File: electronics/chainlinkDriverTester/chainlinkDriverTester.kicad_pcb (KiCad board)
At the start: 2 copper layers, 198.1 x 30.5 mm, 69 parts, among them J1 Inputs, J10 Sensor C, J11 Sensor D, J12 Motor E, J13 Motor F, J14 Sensor E, J15 Sensor F, J16 Power, J17 Power, J18 Power, J19 Outputs, J2 Inputs, J20 Outputs, J21 Outputs, J3 Motor A, J4 Inputs, J5 Motor B, J6 Motor C, J7 Motor D, J8 Sensor A, J9 Sensor B, U1 74HC595, U10 TPL7407L, U2 TPL7407L, U3 74HC125, U4 74HC165, U5 74HC595, U6 TPL7407L, U7 74HC595, U8 TPL7407L, U9 74HC595

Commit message: Checkpoint
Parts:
- removed C10, C11, C12, C9: 0.1uF, Capacitor_SMD:C_0603_1608Metric
- removed C8: 10uF, Capacitor_SMD:CP_Elec_4x5.3
- removed D4: LED D, ModifiedSymbols:LED_0603_1608Metric_Silkscreen
- removed D5: LED E, ModifiedSymbols:LED_0603_1608Metric_Silkscreen
- removed D6: LED F, ModifiedSymbols:LED_0603_1608Metric_Silkscreen
- removed J1, J2, J4: Inputs, ScrewTerminals:C8465_WJ500V-5.08-2P
- removed J16, J17, J18: Power, ScrewTerminals:C8465_WJ500V-5.08-2P
- removed J19, J20, J21: Outputs, ScrewTerminals:C8465_WJ500V-5.08-2P
- removed R13: 0R, Resistor_SMD:R_0603_1608Metric
- removed U10, U6, U8: TPL7407L, ModifiedSymbols:SOIC-16_3.9x9.9mm_P1.27mm_silk
- removed U7, U9: 74HC595, ModifiedSymbols:SOIC-16_3.9x9.9mm_P1.27mm_silk
- added F1: 50mA (0ZCM0005FF2G), Fuse:Fuse_0603_1608Metric, F.Cu at (115.6, 105.4)
- added F2: Fuse Holder BK-6013, BK-6013:BK-6013, F.Cu at (120.7, 35.6)
- added H10: MountingHole, MountingHole:MountingHole_3.2mm_M3_ISO7380_Pad, F.Cu at (31.8, 68.6)
- added H11: MountingHole, MountingHole:MountingHole_3.2mm_M3_ISO7380_Pad, F.Cu at (91.4, 68.6)
- added H12: MountingHole, MountingHole:MountingHole_3.2mm_M3_ISO7380_Pad, F.Cu at (124.5, 68.6)
- added H13: MountingHole, MountingHole:MountingHole_3.2mm_M3_ISO7380_Pad, F.Cu at (157.5, 68.6)
- added H14: MountingHole, MountingHole:MountingHole_3.2mm_M3_ISO7380_Pad, F.Cu at (217.2, 68.6)
- added H15: MountingHole, MountingHole:MountingHole_3.2mm_M3_ISO7380_Pad, F.Cu at (124.5, 29.2)
- added H16: MountingHole, MountingHole:MountingHole_3.2mm_M3_ISO7380_Pad, F.Cu at (124.5, 116.8)
- added H8: MountingHole, MountingHole:MountingHole_3.2mm_M3_ISO7380_Pad, F.Cu at (29.2, 116.8)
- added H9: MountingHole, MountingHole:MountingHole_3.2mm_M3_ISO7380_Pad, F.Cu at (219.7, 116.8)
- added J22: Power, ScrewTerminals:C8465_WJ500V-5.08-2P, F.Cu at (108.0, 34.3)
- added J26: exp, Connector_PinHeader_2.54mm:PinHeader_1x04_P2.54mm_Vertical, F.Cu at (134.6, 108.6)
- added J27: exp, Connector_PinHeader_2.54mm:PinHeader_1x04_P2.54mm_Vertical, F.Cu at (134.6, 111.1)
- added J28: exp, Connector_PinHeader_2.54mm:PinHeader_1x04_P2.54mm_Vertical, F.Cu at (134.6, 113.7)
- added J29: exp, Connector_PinHeader_2.54mm:PinHeader_1x04_P2.54mm_Vertical, F.Cu at (147.3, 108.6)
- added J30: exp, Connector_PinHeader_2.54mm:PinHeader_1x04_P2.54mm_Vertical, F.Cu at (147.3, 111.1)
- added J31: exp, Connector_PinHeader_2.54mm:PinHeader_1x04_P2.54mm_Vertical, F.Cu at (147.3, 113.7)
- added J32: Conn_01x06_Female, Connector_PinSocket_2.54mm:PinSocket_1x06_P2.54mm_Vertical, F.Cu at (28.6, 36.8)
- added TP1: TestPoint, pogoPins:pogo1mm, F.Cu at (198.1, 74.9)
- added TP10: TestPoint, pogoPins:pogo1mm, F.Cu at (200.7, 57.1)
- added TP11: TestPoint, pogoPins:pogo1mm, F.Cu at (181.6, 57.1)
- added TP12: TestPoint, pogoPins:pogo1mm, F.Cu at (162.6, 57.1)
- added TP13: TestPoint, pogoPins:pogo1mm, F.Cu at (96.5, 57.1)
- added TP14: TestPoint, pogoPins:pogo1mm, F.Cu at (77.5, 57.1)
- added TP15: TestPoint, pogoPins:pogo1mm, F.Cu at (58.4, 57.1)
- added TP16: TestPoint, pogoPins:pogo1mm, F.Cu at (198.2, 57.1)
- added TP17: TestPoint, pogoPins:pogo1mm, F.Cu at (179.1, 57.1)
- added TP18: TestPoint, pogoPins:pogo1mm, F.Cu at (160.1, 57.1)
- added TP19: TestPoint, pogoPins:pogo1mm, F.Cu at (94.0, 57.1)
- added TP2: TestPoint, pogoPins:pogo1mm, F.Cu at (195.6, 74.9)
- added TP20: TestPoint, pogoPins:pogo1mm, F.Cu at (75.0, 57.1)
- added TP21: TestPoint, pogoPins:pogo1mm, F.Cu at (55.9, 57.1)
- added TP22: TestPoint, pogoPins:pogo1mm, F.Cu at (94.0, 74.9)
- added TP23: TestPoint, pogoPins:pogo1mm, F.Cu at (195.7, 57.1)
- added TP24: TestPoint, pogoPins:pogo1mm, F.Cu at (176.6, 57.1)
- added TP25: TestPoint, pogoPins:pogo1mm, F.Cu at (157.6, 57.1)
- added TP26: TestPoint, pogoPins:pogo1mm, F.Cu at (91.5, 57.1)
- added TP27: TestPoint, pogoPins:pogo1mm, F.Cu at (72.5, 57.1)
- added TP28: TestPoint, pogoPins:pogo1mm, F.Cu at (53.4, 57.1)
- added TP29: TestPoint, pogoPins:pogo1mm, F.Cu at (91.4, 74.9)
- added TP3: TestPoint, pogoPins:pogo1mm, F.Cu at (193.0, 74.9)
- added TP30: TestPoint, pogoPins:pogo1mm, F.Cu at (193.2, 57.1)
- added TP31: TestPoint, pogoPins:pogo1mm, F.Cu at (174.1, 57.1)
- added TP32: TestPoint, pogoPins:pogo1mm, F.Cu at (155.1, 57.1)
- added TP33: TestPoint, pogoPins:pogo1mm, F.Cu at (89.0, 57.1)
- added TP34: TestPoint, pogoPins:pogo1mm, F.Cu at (70.0, 57.1)
- added TP35: TestPoint, pogoPins:pogo1mm, F.Cu at (50.9, 57.1)
- added TP36: TestPoint, pogoPins:pogo1mm, F.Cu at (88.9, 74.9)
- added TP37: TestPoint, pogoPins:pogo1mm, F.Cu at (190.7, 57.1)
- added TP38: TestPoint, pogoPins:pogo1mm, F.Cu at (171.6, 57.1)
- added TP39: TestPoint, pogoPins:pogo1mm, F.Cu at (152.6, 57.1)
- added TP4: TestPoint, pogoPins:pogo1mm, F.Cu at (179.1, 74.9)
- added TP40: TestPoint, pogoPins:pogo1mm, F.Cu at (86.5, 57.1)
- added TP41: TestPoint, pogoPins:pogo1mm, F.Cu at (67.5, 57.1)
- added TP42: TestPoint, pogoPins:pogo1mm, F.Cu at (48.4, 57.1)
- added TP43: TestPoint, pogoPins:pogo1mm, F.Cu at (74.9, 74.9)
- added TP44: TestPoint, pogoPins:pogo1mm, F.Cu at (72.4, 74.9)
- added TP45: TestPoint, pogoPins:pogo1mm, F.Cu at (69.8, 74.9)
- added TP46: TestPoint, pogoPins:pogo1mm, F.Cu at (55.9, 74.9)
- added TP47: TestPoint, pogoPins:pogo1mm, F.Cu at (53.3, 74.9)
- added TP48: TestPoint, pogoPins:pogo1mm, F.Cu at (50.8, 74.9)
- added TP49: TestPoint, pogoPins:pogo2mm, F.Cu at (209.6, 55.9)
- added TP5: TestPoint, pogoPins:pogo1mm, F.Cu at (176.5, 74.9)
- added TP50: TestPoint, pogoPins:pogo2mm, F.Cu at (39.4, 55.9)
- added TP51: TestPoint, pogoPins:pogo2mm, F.Cu at (209.6, 61.0)
- added TP52: TestPoint, pogoPins:pogo2mm, F.Cu at (39.4, 61.0)
- added TP53: TestPoint, pogoPins:pogo2mm, F.Cu at (209.6, 66.0)
- added TP54: TestPoint, pogoPins:pogo2mm, F.Cu at (39.4, 66.0)
- added TP55: TestPoint, pogoPins:pogo2mm, F.Cu at (209.6, 71.1)
- added TP56: TestPoint, pogoPins:pogo2mm, F.Cu at (39.4, 71.1)
- added TP57: TestPoint, pogoPins:pogo2mm, F.Cu at (209.6, 76.2)
- added TP58: TestPoint, pogoPins:pogo2mm, F.Cu at (39.4, 76.2)
- added TP59: TestPoint, pogoPins:pogo2mm, F.Cu at (209.6, 81.3)
- added TP6: TestPoint, pogoPins:pogo1mm, F.Cu at (174.0, 74.9)
- added TP60: TestPoint, pogoPins:pogo2mm, F.Cu at (39.4, 81.3)
- added TP61: TestPoint, TestPoint:TestPoint_THTPad_D2.0mm_Drill1.0mm, F.Cu at (144.8, 92.7)
- added TP62: TestPoint, TestPoint:TestPoint_THTPad_D2.0mm_Drill1.0mm, F.Cu at (142.2, 92.7)
- added TP63: TestPoint, pogoPins:pogo2mm, F.Cu at (111.8, 59.7)
- added TP64: TestPoint, pogoPins:pogo2mm, F.Cu at (116.8, 59.7)
- added TP65: TestPoint, pogoPins:pogo2mm, F.Cu at (121.9, 59.7)
- added TP66: TestPoint, pogoPins:pogo2mm, F.Cu at (127.0, 59.7)
- added TP67: TestPoint, pogoPins:pogo2mm, F.Cu at (132.1, 59.7)
- added TP68: TestPoint, pogoPins:pogo2mm, F.Cu at (137.2, 59.7)
- added TP69: TestPoint, TestPoint:TestPoint_THTPad_D2.0mm_Drill1.0mm, F.Cu at (181.6, 91.4)
- added TP7: TestPoint, pogoPins:pogo1mm, F.Cu at (160.0, 74.9)
- added TP70: TestPoint, TestPoint:TestPoint_THTPad_D2.0mm_Drill1.0mm, F.Cu at (186.7, 91.4)
- added TP71: TestPoint, TestPoint:TestPoint_THTPad_D2.0mm_Drill1.0mm, F.Cu at (194.3, 114.3)
- added TP72: TestPoint, TestPoint:TestPoint_THTPad_D2.0mm_Drill1.0mm, F.Cu at (199.4, 114.3)
- added TP73: TestPoint, TestPoint:TestPoint_THTPad_D2.0mm_Drill1.0mm, F.Cu at (207.0, 91.4)
- added TP74: TestPoint, TestPoint:TestPoint_THTPad_D2.0mm_Drill1.0mm, F.Cu at (109.2, 106.7)
- added TP75: TestPoint, TestPoint:TestPoint_THTPad_D2.0mm_Drill1.0mm, F.Cu at (207.0, 114.3)
- added TP8: TestPoint, pogoPins:pogo1mm, F.Cu at (157.5, 74.9)
- added TP9: TestPoint, pogoPins:pogo1mm, F.Cu at (154.9, 74.9)
- C1, C5: value 0.1uF -> 10uF; footprint Capacitor_SMD:C_0603_1608Metric -> Capacitor_SMD:CP_Elec_4x5.3
- C2, C4: value 0.1uF -> 4.7uF; footprint Capacitor_SMD:C_0603_1608Metric -> Capacitor_SMD:C_0805_2012Metric
- C6, C7: footprint Capacitor_SMD:C_0603_1608Metric -> Capacitor_SMD:C_0805_2012Metric
- D1: value LED A -> Red; footprint ModifiedSymbols:LED_0603_1608Metric_Silkscreen -> LED_SMD:LED_0805_2012Metric
- D2: value LED B -> Red; footprint ModifiedSymbols:LED_0603_1608Metric_Silkscreen -> LED_SMD:LED_0805_2012Metric
- D3: value LED C -> 1N5819; footprint ModifiedSymbols:LED_0603_1608Metric_Silkscreen -> Diode_SMD:D_SOD-123
- H6, H7: footprint JLCPCB:AssemblyToolingHole -> MountingHole:MountingHole_3.2mm_M3_ISO7380_Pad
- R1, R2: value 220R -> 1k; footprint Resistor_SMD:R_0603_1608Metric -> Resistor_SMD:R_0805_2012Metric
- R10, R3, R4, R5: value 220R -> 15k; footprint Resistor_SMD:R_0603_1608Metric -> Resistor_SMD:R_0805_2012Metric
- R11, R7: value 47k -> 220; footprint Resistor_SMD:R_0603_1608Metric -> Resistor_SMD:R_0805_2012Metric
- R12: value 47k -> 0.01R 1% 1W; footprint Resistor_SMD:R_0603_1608Metric -> Resistor_SMD:R_0612_1632Metric
- R6: value 47k -> 15k; footprint Resistor_SMD:R_0603_1608Metric -> Resistor_SMD:R_0805_2012Metric
- R8: value 47k -> 1k; footprint Resistor_SMD:R_0603_1608Metric -> Resistor_SMD:R_0805_2012Metric
- R9: value 47k -> 2k; footprint Resistor_SMD:R_0603_1608Metric -> Resistor_SMD:R_0805_2012Metric
- U1: value 74HC595 -> AP7361C-33E; footprint ModifiedSymbols:SOIC-16_3.9x9.9mm_P1.27mm_silk -> Package_TO_SOT_SMD:SOT-223-3_TabPin2
- U2: value TPL7407L -> TTGO_TDisplay; footprint ModifiedSymbols:SOIC-16_3.9x9.9mm_P1.27mm_silk -> ESP32:T-DISPLAY
- U3: value 74HC125 -> VN7007ALH; footprint ModifiedSymbols:SOIC-14_3.9x8.7mm_P1.27mm_silk -> VN7007ALHTR:VN7007ALHTR
- U4: value 74HC165 -> MCP23017_SS; footprint ModifiedSymbols:SOIC-16_3.9x9.9mm_P1.27mm_silk -> Package_SO:SSOP-28_5.3x10.2mm_P0.65mm
- U5: value 74HC595 -> INA219BxD; footprint ModifiedSymbols:SOIC-16_3.9x9.9mm_P1.27mm_silk -> Package_SO:SOIC-8_3.9x4.9mm_P1.27mm
- moved C1 115.9 mm to (104.1, 98.4), turned to 270 degrees
- moved U1 105.0 mm to (96.5, 98.4)
- moved C4 102.4 mm to (123.2, 106.7)
- moved R1 99.0 mm to (156.2, 118.1), turned to 90 degrees
- moved C5 95.0 mm to (87.6, 97.8), turned to 270 degrees
- moved U3 89.7 mm to (139.7, 33.0), turned to 90 degrees
- moved U2 82.7 mm to (179.1, 118.1)
- moved R12 82.5 mm to (137.2, 44.5), turned to 270 degrees
- moved R11 73.9 mm to (147.3, 50.8), turned to 180 degrees
- moved R2 69.9 mm to (161.3, 118.1), turned to 90 degrees
- moved R10 67.3 mm to (115.6, 94.6), turned to 90 degrees
- moved C2 65.9 mm to (128.3, 106.7), turned to 0 degrees
- moved C6 63.7 mm to (131.4, 96.5)
- moved C7 62.7 mm to (125.7, 47.0), turned to 270 degrees
- moved R4 58.9 mm to (111.8, 96.5), turned to 90 degrees
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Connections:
- C1 pad 1: GND -> +5V
- C1 pad 2: +12V -> GND
- C2 pad 1: +3V3 -> GND
- C2 pad 2: GND -> +5V
- C4 pad 1: +3V3 -> GND
- C4 pad 2: GND -> Net-(C4-Pad2)
- C5 pad 1: +3V3 -> Net-(C4-Pad2)
- C7 pad 1: +3V3 -> GND
- C7 pad 2: GND -> +3V3
- D1 pad 1: GND -> Net-(D1-Pad1)
- D1 pad 2: Net-(D1-Pad2) -> /12V_EN
- D2 pad 1: GND -> Net-(D2-Pad1)
- D3 pad 1: GND -> Net-(D2-Pad2)
- J10 pad 1: GND -> /SENSOR_C_GND
- J10 pad 2: +3V3 -> /SENSOR_C_VCC
- J10 pad 3: /SENSOR_C -> /SENSOR_C_SIGNAL
- J11 pad 1: GND -> /SENSOR_D_GND
- J11 pad 2: +3V3 -> /SENSOR_D_VCC
- J11 pad 3: /SENSOR_D -> /SENSOR_D_SIGNAL
- J12 pad 5: +12V -> /OUT_E_COMMON
- J13 pad 5: +12V -> /OUT_F_COMMON
- J14 pad 1: GND -> /SENSOR_E_GND
- J14 pad 2: +3V3 -> /SENSOR_E_VCC
- J14 pad 3: /SENSOR_E -> /SENSOR_E_SIGNAL
- J15 pad 1: GND -> /SENSOR_F_GND
- J15 pad 2: +3V3 -> /SENSOR_F_VCC
- J15 pad 3: /SENSOR_F -> /SENSOR_F_SIGNAL
- J3 pad 5: +12V -> /OUT_A_COMMON
- J5 pad 5: +12V -> /OUT_B_COMMON
- J6 pad 5: +12V -> /OUT_C_COMMON
- J7 pad 5: +12V -> /OUT_D_COMMON
- J8 pad 1: GND -> /SENSOR_A_GND
- J8 pad 2: +3V3 -> /SENSOR_A_VCC
- J8 pad 3: /SENSOR_A -> /SENSOR_A_SIGNAL
- J9 pad 1: GND -> /SENSOR_B_GND
- J9 pad 2: +3V3 -> /SENSOR_B_VCC
- J9 pad 3: /SENSOR_B -> /SENSOR_B_SIGNAL
- R1 pad 1: Net-(D5-Pad2) -> +3V3
- R1 pad 2: /LED_E -> /SDA
- R10 pad 1: Net-(D6-Pad2) -> /MCP_RESET
- R10 pad 2: /LED_F -> GND
- R11 pad 1: +3V3 -> /12V_TEST_FEED
- R11 pad 2: /SENSOR_E -> Net-(D3-Pad2)
- R12 pad 1: +3V3 -> Net-(D2-Pad2)
- R12 pad 2: /SENSOR_F -> /12V_OUTPUT
- R2 pad 1: Net-(D1-Pad2) -> +3V3
- R2 pad 2: /LED_A -> /SCL
- R3 pad 1: Net-(D2-Pad2) -> Net-(R3-Pad1)
- R3 pad 2: /LED_B -> /12V_EN
- R4 pad 1: Net-(D3-Pad2) -> /MCP_INT
- R4 pad 2: /LED_C -> +3V3
- R5 pad 1: Net-(D4-Pad2) -> GND
- R5 pad 2: /LED_D -> /12V_EN
- R6 pad 1: +3V3 -> GND
- R6 pad 2: /SENSOR_A -> Net-(R6-Pad2)
- R7 pad 1: +3V3 -> GND
- R7 pad 2: /SENSOR_B -> Net-(D1-Pad1)
- R8 pad 1: +3V3 -> GND
- R8 pad 2: /SENSOR_C -> Net-(R8-Pad2)
- R9 pad 1: +3V3 -> GND
- R9 pad 2: /SENSOR_D -> Net-(D2-Pad1)
- U1 pad 1: /MOTOR_A_PHASE_B -> +5V
- U1 pad 2: /MOTOR_A_PHASE_C -> GND
- U1 pad 3: /MOTOR_A_PHASE_D -> Net-(C4-Pad2)
- U2 pad 1: /MOTOR_B_PHASE_B -> GND
- U2 pad 10: (no net) -> GND
- U2 pad 11: /OUT_A_PHASE_A -> GND
- U2 pad 12: /OUT_A_PHASE_B -> +3V3
- U2 pad 13: /OUT_A_PHASE_C -> +5V
- U2 pad 14: /OUT_A_PHASE_D -> GND
- U2 pad 15: /OUT_B_PHASE_A -> /12V_TEST_FEED
- U2 pad 16: /OUT_B_PHASE_B -> /MCP_RESET
- U2 pad 2: /MOTOR_B_PHASE_A -> GND
- U2 pad 3: /MOTOR_A_PHASE_D -> /12V_EN
- U2 pad 4: /MOTOR_A_PHASE_C -> /3V3_FUSED
- U2 pad 5: /MOTOR_A_PHASE_B -> /SENSOR_LATCH
- U2 pad 6: /MOTOR_A_PHASE_A -> /SDA
- U2 pad 7: GND -> Net-(TP71-Pad1)
- U2 pad 8: GND -> /SCL
- U2 pad 9: +12V -> Net-(TP72-Pad1)
- U3 pad 1: GND -> Net-(D2-Pad2)
- U3 pad 2: /CLOCK_IN -> Net-(D2-Pad2)
- U3 pad 3: /CLOCK_OUT -> Net-(D2-Pad2)
- U3 pad 4: GND -> Net-(R3-Pad1)
- U3 pad 5: /MOTOR_LATCH_IN -> Net-(R8-Pad2)
- U3 pad 6: /MOTOR_LATCH_OUT -> Net-(R6-Pad2)
- U4 pad 1: /SENSOR_LATCH_IN -> /SENSOR_A_SIGNAL
- U4 pad 10: /SENSOR_IN -> GND
- U4 pad 11: /SENSOR_A -> (no net)
- U4 pad 12: /SENSOR_B -> /SCL
- U4 pad 13: /SENSOR_C -> /SDA
- U4 pad 14: /SENSOR_D -> (no net)
- U4 pad 16: +3V3 -> GND
- U4 pad 2: /CLOCK_IN -> /SENSOR_B_SIGNAL
- U4 pad 3: /SENSOR_E -> /SENSOR_C_SIGNAL
- U4 pad 4: /SENSOR_F -> /SENSOR_D_SIGNAL
- U4 pad 5: /LOOPBACK_A -> /SENSOR_E_SIGNAL
- U4 pad 6: /LOOPBACK_B -> /SENSOR_F_SIGNAL
- U4 pad 7: (no net) -> Net-(TP61-Pad1)
- U4 pad 8: GND -> Net-(TP62-Pad1)
- U4 pad 9: /SENSOR_OUT -> +3V3
- U5 pad 1: /MOTOR_C_PHASE_B -> GND
- U5 pad 2: /MOTOR_C_PHASE_C -> GND
- U5 pad 3: /MOTOR_C_PHASE_D -> /SDA
- U5 pad 4: /LED_A -> /SCL
- U5 pad 5: /LED_B -> +3V3
- U5 pad 6: /LED_C -> GND
- U5 pad 7: /LOOPBACK_A -> /12V_OUTPUT
- U5 pad 8: GND -> Net-(D2-Pad2)
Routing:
- net +3V3: track 267.1 -> 0.00 mm, vias 18 -> 0
- net +12V: track 226.3 -> 0.00 mm
- net /CLOCK_IN: track 196.4 -> 0.00 mm
- net /MOTOR_LATCH_IN: track 193.0 -> 0.00 mm, vias 5 -> 0
- net /SENSOR_LATCH_IN: track 173.4 -> 0.00 mm, vias 3 -> 0
- net /SENSOR_IN: track 126.0 -> 28.6 mm
- net /SENSOR_F: track 92.1 -> 0.00 mm
- net /LED_A: track 88.0 -> 0.00 mm, vias 2 -> 0
- net GND: track 78.3 -> 0.00 mm, vias 66 -> 0
- net /SENSOR_E: track 72.5 -> 0.00 mm
- net /SENSOR_OUT: track 69.1 -> 0.00 mm
- net /LED_B: track 66.3 -> 0.00 mm, vias 2 -> 0
- net /SENSOR_D: track 57.8 -> 0.00 mm
- net /SENSOR_F_SIGNAL: track 0.00 -> 55.3 mm
- net /LOOPBACK_B: track 55.3 -> 0.00 mm, vias 2 -> 0
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- added copper zone on B.Cu, net /SW_IN
- added copper zone on F.Cu, net /SW_IN
- removed copper zone on B.Cu, net +12V
- removed copper zone on F.Cu, net +12V
- removed copper zone on F.Cu, net GND
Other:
- board size 198.1 x 30.5 mm -> 198.1 x 95.2 mm
- net class motor added: clearance 0.2, trace_width 0.8, via_dia 0.8, via_drill 0.4
- board text added: "Splitflap Chainlink Driver Tester"
- board text removed: "CLK"
- board text removed: "GND"
- board text removed: "Input"
- board text removed: "Logic 3.3-5V"
- board text removed: "MD"
- board text removed: "ML"
- board text removed: "Motor 5-12V"
- board text removed: "Output"
- board text removed: "Power"
- board text removed: "SD"
- board text removed: "SL"
- board text removed: "Splitflap Chainlink Driver"

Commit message: Checkpoint. Placement done, starting routing
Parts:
- added D4: Red, LED_SMD:LED_0805_2012Metric, F.Cu at (123.2, 94.0)
- added R13: 220, Resistor_SMD:R_0805_2012Metric, F.Cu at (127.0, 94.0)
- moved R10 45.5 mm to (160.0, 104.1)
- moved R4 45.5 mm to (156.2, 106.0)
- moved C1 30.6 mm to (134.6, 101.0)
- moved U1 28.8 mm to (125.1, 101.6)
- moved C5 28.1 mm to (115.6, 101.0)
- moved R2 22.4 mm to (160.3, 95.8)
- moved R1 20.8 mm to (157.0, 97.3)
- moved R9 17.6 mm to (141.0, 48.3), turned to 90 degrees
- moved R11 15.5 mm to (132.1, 48.3), turned to 0 degrees
- moved C6 13.1 mm to (144.1, 99.8), turned to 180 degrees
- moved F1 10.9 mm to (119.4, 95.2)
- moved J32 9.44 mm to (35.6, 30.5)
- moved D2 9.38 mm to (141.0, 44.5), turned to 90 degrees
- moved TP74 9.09 mm to (111.1, 97.8)
- moved D3 9.09 mm to (132.7, 44.5)
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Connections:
- U4 pad 4: /SENSOR_D_SIGNAL -> Net-(TP61-Pad1)
- U4 pad 5: /SENSOR_E_SIGNAL -> Net-(TP62-Pad1)
- U4 pad 6: /SENSOR_F_SIGNAL -> /SENSOR_D_SIGNAL
- U4 pad 7: Net-(TP61-Pad1) -> /SENSOR_E_SIGNAL
- U4 pad 8: Net-(TP62-Pad1) -> /SENSOR_F_SIGNAL
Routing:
- net /SENSOR_E_SIGNAL: track 0.00 -> 142.5 mm, vias 0 -> 1
- net /SENSOR_D_SIGNAL: track 0.00 -> 134.1 mm, vias 0 -> 1
- net /SENSOR_F_SIGNAL: track 55.3 -> 161.7 mm, vias 0 -> 1
- net /12V_EN: track 0.00 -> 104.8 mm, vias 0 -> 1
- net /12V_TEST_FEED: track 0.00 -> 100.1 mm, vias 0 -> 2
- net +5V: track 0.00 -> 98.3 mm
- net GND: track 0.00 -> 59.4 mm, vias 0 -> 16
- net /SENSOR_C_GND: track 0.00 -> 55.9 mm
- net /SENSOR_LATCH: track 0.00 -> 54.8 mm, vias 0 -> 1
- net /SENSOR_B_GND: track 0.00 -> 53.9 mm
- net /SENSOR_A_SIGNAL: track 0.00 -> 53.7 mm
- net /SENSOR_C_VCC: track 0.00 -> 52.9 mm
- net /SENSOR_D_VCC: track 0.00 -> 52.6 mm
- net /SENSOR_E_VCC: track 0.00 -> 52.3 mm
- net /SENSOR_B_VCC: track 0.00 -> 52.1 mm
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- added copper zone on F.Cu, net /12V_OUTPUT
- added copper zone on F.Cu, net Net-(D2-Pad2)
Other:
- outline, holes or cut-outs redrawn

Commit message: Finished routing
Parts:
- removed TP72: TestPoint, TestPoint:TestPoint_THTPad_D2.0mm_Drill1.0mm
- added C10: 0.1uF, Capacitor_SMD:C_0805_2012Metric, F.Cu at (117.5, 84.5)
- added C8: 0.1uF, Capacitor_SMD:C_0805_2012Metric, F.Cu at (108.0, 61.0)
- added C9: 0.1uF, Capacitor_SMD:C_0805_2012Metric, F.Cu at (109.7, 93.2)
- added D5: WS2812B, LED_SMD:LED_WS2812B_PLCC4_5.0x5.0mm_P3.2mm, F.Cu at (112.4, 84.6)
- added D6: WS2812B, LED_SMD:LED_WS2812B_PLCC4_5.0x5.0mm_P3.2mm, F.Cu at (102.9, 60.3)
- added U6: SN74LV1T34DBV, Package_TO_SOT_SMD:SOT-23-5, F.Cu at (114.3, 92.2)
- TP69, TP70, TP71, TP73, TP75: moved to B.Cu
- moved TP75 33.1 mm to (179.1, 97.8)
- moved R4 28.7 mm to (181.6, 92.7), turned to 180 degrees
- moved R10 23.4 mm to (137.2, 109.2), turned to 180 degrees
- moved R2 8.98 mm to (156.5, 103.9), turned to 180 degrees
- moved R1 5.00 mm to (159.0, 101.9), turned to 180 degrees
- moved H11 2.54 mm to (91.4, 66.0)
- moved H13 2.54 mm to (157.5, 66.0)
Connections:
- U2 pad 12: +3V3 -> (no net)
- U2 pad 9: Net-(TP72-Pad1) -> /LED
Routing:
- net /LED: track 0.00 -> 136.9 mm
- net /3V3_FUSED: track 45.2 -> 174.6 mm, vias 1 -> 2
- net /SCL: track 26.4 -> 153.5 mm, vias 1 -> 4
- net /SDA: track 27.9 -> 153.0 mm, vias 1 -> 4
- net +3V3: track 39.5 -> 164.2 mm, vias 1 -> 4
- net /MCP_RESET: track 0.00 -> 79.1 mm
- net +5V: track 98.3 -> 162.8 mm, vias 0 -> 2
- net /MCP_INT: track 0.00 -> 61.4 mm, vias 0 -> 1
- net /SENSOR_A_SIGNAL: track 53.7 -> 114.4 mm, vias 0 -> 1
- net /SENSOR_B_SIGNAL: track 50.3 -> 92.2 mm, vias 0 -> 1
- net Net-(D5-Pad2): track 0.00 -> 41.8 mm
- net /SENSOR_C_SIGNAL: track 50.1 -> 83.0 mm, vias 0 -> 1
- net /12V_EN: track 104.8 -> 132.8 mm, vias 1 -> 3
- net /SENSOR_DATA: track 24.3 -> 39.7 mm, vias 0 -> 1
- net /MOTOR_DATA: track 30.1 -> 42.1 mm, vias 0 -> 1
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
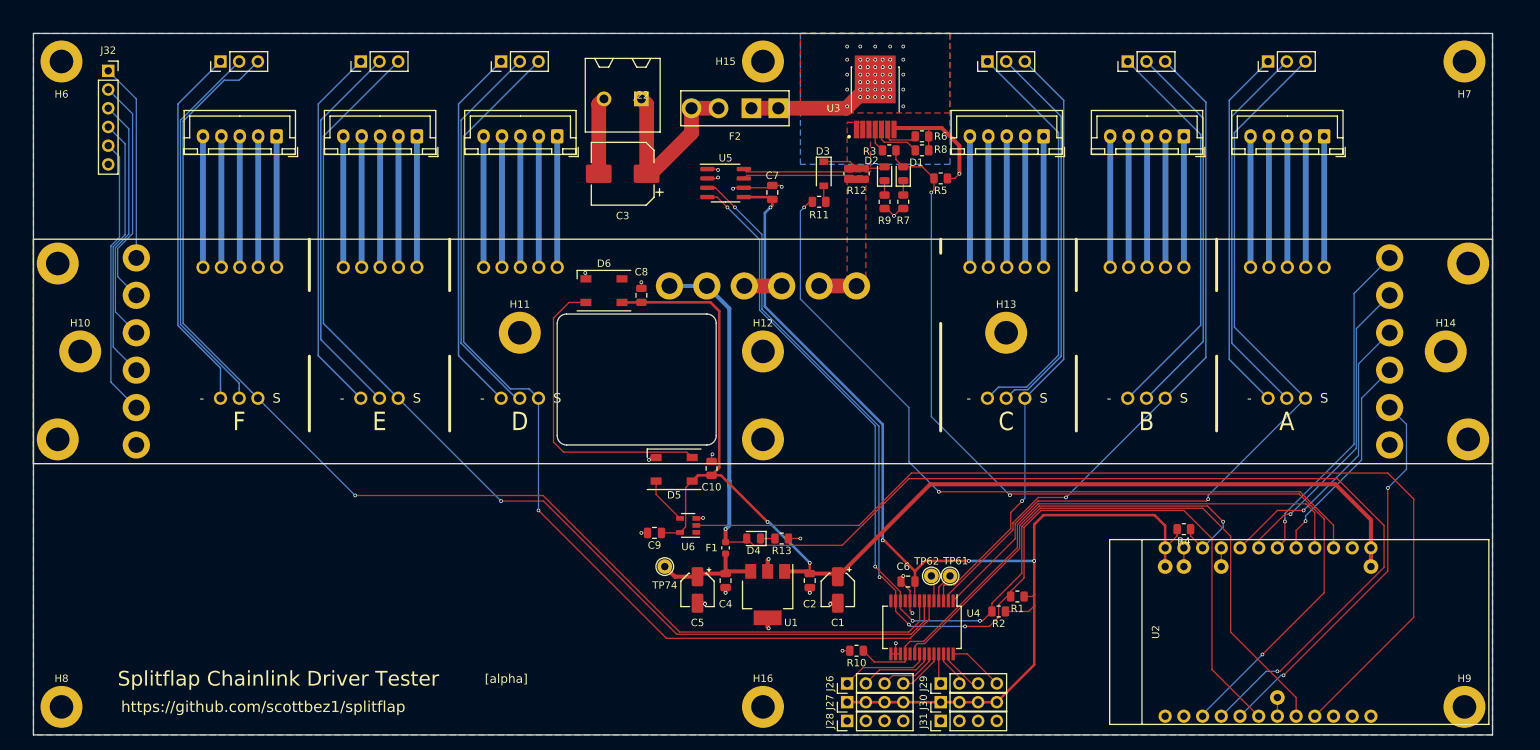
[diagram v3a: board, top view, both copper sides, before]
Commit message: PCB updates, add buzzer, add CI
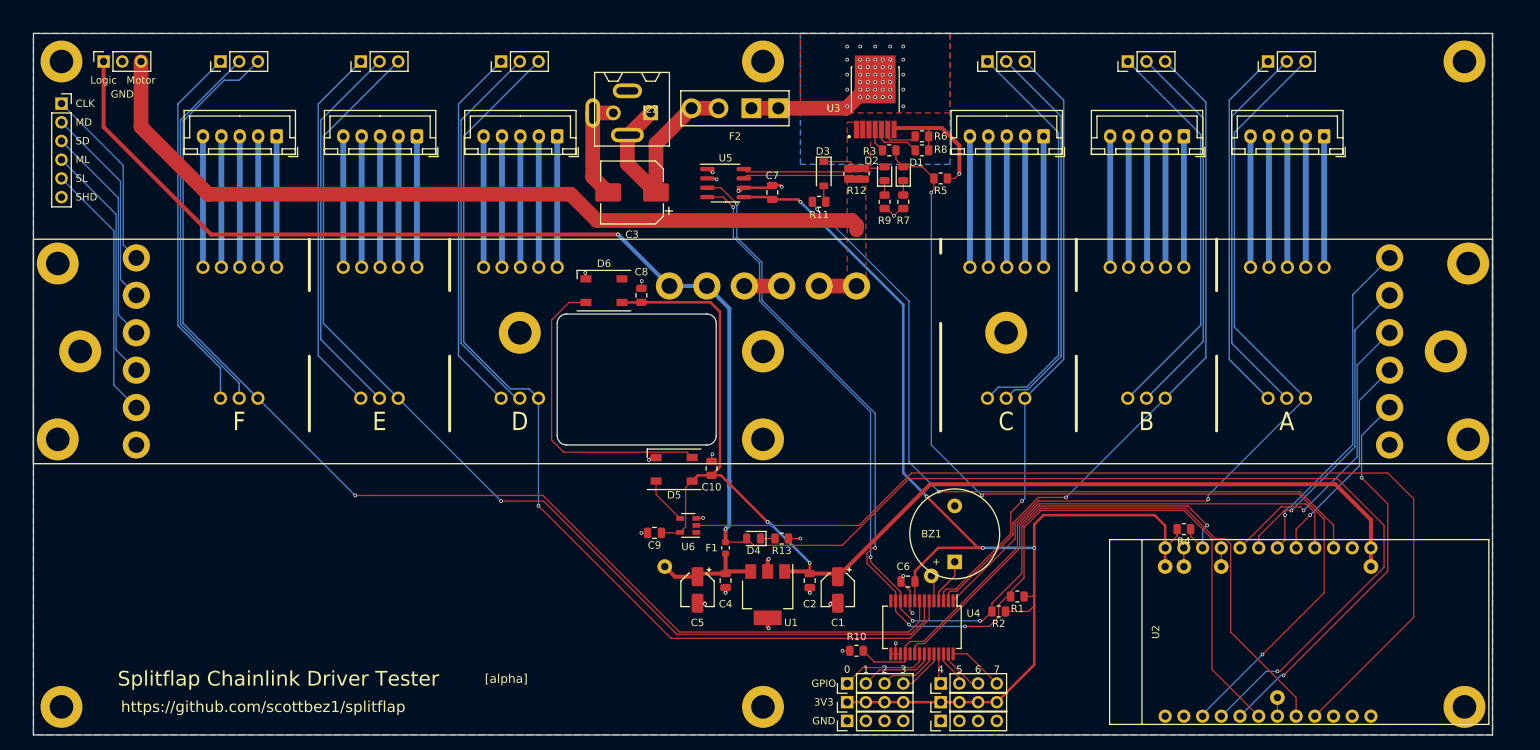
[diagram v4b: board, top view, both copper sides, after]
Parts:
- removed TP61: TestPoint, TestPoint:TestPoint_THTPad_D2.0mm_Drill1.0mm
- added BZ1: Buzzer, Buzzer_Beeper:Buzzer_12x9.5RM7.6, F.Cu at (150.5, 97.2)
- added J1: Barrel_Jack_Switch, PJ-202A:PJ-202A, F.Cu at (106.0, 36.2)
- added J2: Conn_01x03_Female, Connector_PinSocket_2.54mm:PinSocket_1x03_P2.54mm_Vertical, F.Cu at (34.9, 29.2)
- H10, H11, H12, H13, H14, H15, H16, H6, H7, H8, H9, TP62, TP74: moved to B.Cu
- moved J32 7.75 mm to (29.2, 34.9)
- moved C3 2.84 mm to (106.7, 47.0)
- moved J22 2.29 mm to (109.2, 36.2)
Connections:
- net Net-(J26-Pad1) renamed /GPA0
- net Net-(J26-Pad2) renamed /GPA1
- net Net-(J26-Pad3) renamed /GPA2
- net Net-(J26-Pad4) renamed /GPA3
- net Net-(J29-Pad1) renamed /GPA4
- net Net-(J29-Pad2) renamed /GPA5
- net Net-(J29-Pad3) renamed /GPA6
- net Net-(J29-Pad4) renamed /GPA7
- U4 pad 4: Net-(TP61-Pad1) -> /BUZZER
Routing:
- net /12V_OUTPUT: track 20.8 -> 133.0 mm
- net /3V3_FUSED: track 174.6 -> 269.3 mm, vias 2 -> 3
- net /BUZZER: track 0.00 -> 6.19 mm
- net +12V: track 25.9 -> 30.9 mm
- net Net-(TP61-Pad1): track 4.02 -> 0.00 mm
- net /MOTOR_OUT: track 31.2 -> 27.7 mm
- net /MCP_INT: track 61.4 -> 58.1 mm
- net /SENSOR_IN: track 33.6 -> 30.2 mm
- net +3V3: track 164.2 -> 167.0 mm
- net GND: track 71.1 -> 73.9 mm
- net /SENSOR_LATCH_OUT: track 38.1 -> 35.3 mm
- net /MOTOR_LATCH_OUT: track 35.9 -> 33.4 mm
- net /12V_EN: track 132.8 -> 135.1 mm
- net /CLOCK_OUT: track 27.0 -> 25.2 mm
- net /12V_TEST_FEED: track 106.6 -> 105.0 mm
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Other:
- board text added: "0"
- board text added: "1"
- board text added: "2"
- board text added: "3"
- board text added: "3V3"
- board text added: "4"
- board text added: "5"
- board text added: "6"
- board text added: "7"
- board text added: "CLK"
- board text added: "GND"
- board text added: "GPIO"
- board text added: "Logic"
- board text added: "MD"
- board text added: "ML"
- board text added: "Motor"
- board text added: "SD"
- board text added: "SHD"
- board text added: "SL"
- board text removed: "-"
- board text removed: "S"

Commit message: Add optional buck module
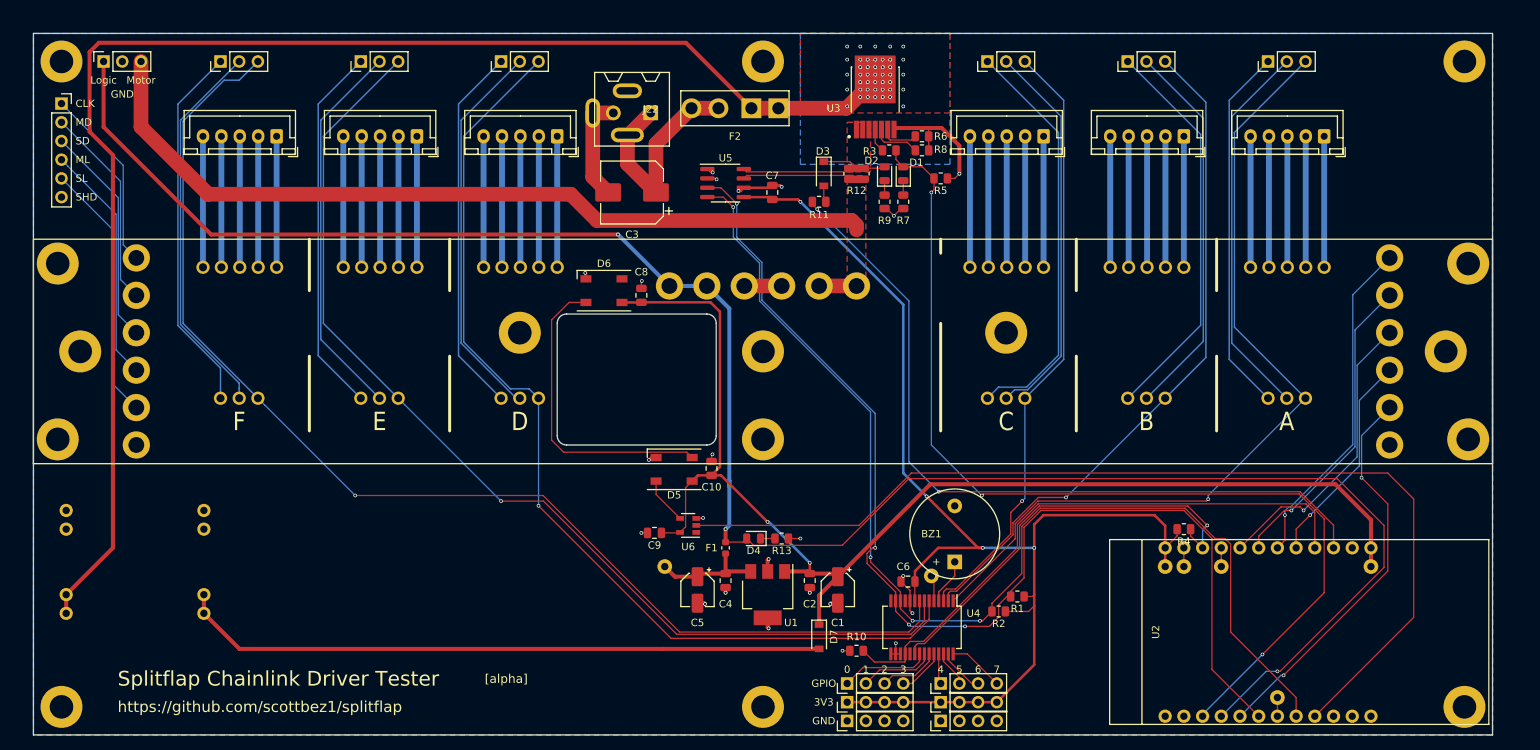
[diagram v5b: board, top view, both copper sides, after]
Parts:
- added D7: 1N5819, Diode_SMD:D_SOD-123, F.Cu at (132.1, 107.3)
- added U7: Buck, Buck:BuckModule, F.Cu at (29.8, 90.2)
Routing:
- net /SW_IN: track 18.4 -> 192.7 mm
- net Net-(D7-Pad2): track 0.00 -> 88.1 mm
- net +5V: track 162.8 -> 170.4 mm

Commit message: Updates
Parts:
- removed C3: 100uF, Capacitor_SMD:CP_Elec_8x10
- added Z101: Fuse, Dummy:Dummy, F.Cu at (124.5, 38.7)
- D1, D2, D4: footprint LED_SMD:LED_0805_2012Metric -> ModifiedSymbols:LED_0805_2012Metric_Silkscreen
- D3, D7: value 1N5819 -> 2A 500mV; footprint Diode_SMD:D_SOD-123 -> Diode_SMD:D_SOD-128
- J22: footprint ScrewTerminals:C8465_WJ500V-5.08-2P -> ScrewTerminals:Generic-5.08-2P
- U7: footprint Buck:BuckModule -> Buck:BuckModuleBackSilk
- moved D3 0.64 mm to (132.7, 43.8)
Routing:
- net +12V: track 30.9 -> 13.9 mm
- net GND: track 73.9 -> 59.4 mm
- net /SDA: track 154.4 -> 153.6 mm
- net /SCL: track 153.3 -> 152.5 mm
- net +5V: track 170.4 -> 169.9 mm
- net /12V_OUTPUT: track 133.0 -> 133.5 mm
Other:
- board text added: "-"
